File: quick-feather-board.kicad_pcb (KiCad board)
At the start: 4 copper layers, 58.4 x 22.9 mm, 100 parts, among them IC1 EOS-S3-QFN, J1 61300211121, J2 1x12_pinhead, J3 1x16_pinhead, J4 S2B-PH-SM4-TB_LF__SN_, J5 0473460001, J6 FTSH-105-01-L-DV-K, J7 61300211121, J8 2x8_pinhead, M1 mounting_pad, M2 mounting_pad, M3 mounting_pad, M4 mounting_pad, Q1 NX3008CBKV, Q2 2N7002PV, Q3 2N7002PV, Q4 DMG1012T-7, U1 TPS62821DLCR, U2 MCP73831T-2ACI_OT, U3 GD25Q16CWIGR, U4 DPS310, U5 MC3635, X1 ECS-_327-12_5-34B-TR

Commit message: Added board pins description and drawings
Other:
- board text added: "GND HEADER_TX HEADER_RX SPI_MST_MISO SPI_MST_MOSI SPI_MST_CLK S3IO_2 S3IO_13 S3IO_25 S3IO_27 ADC1 n.c. GND n.c. 3V3 SYS_RST"
- board text added: "IO_27 IO_32 IO_33 IO_20 IO_19 IO_17 IO_16 IO_43 IO_3 IO_0 IO_1"
- board text added: "IO_28 IO_23 IO_31 IO_12 IO_5 IO_7 IO_10"
- board text added: "IO_29 IO_24 IO_11 IO_4 IO_8 IO_40"
- board text added: "IO_44 IO_45 IO_36 IO_38 IO_34 IO_2 IO_13 IO_25 IO_27"
- board text added: "PDM_CKO I2S_DOUT S3IO_11 S3IO_4 USR_BUTTON S3IO_8 S3IO_40 GND"
- board text added: "PDM_DATA I2S_WCLK I2S_CLK S3IO_12 S3IO_5 S3IO_7 S3IO_10 3V3"
- board text added: "R IO_22 B IO_18 G IO_21"
- board text added: "VBAT SPI_MST_CS2 S3IO_32_I2C1 S3IO_33_I2C1 SPI_SLV_CSn SPI_SLV_MOSI SPI_SLV_MISO SPI_SLV_CLK HEADER_P6 IMU_INT I2C_SCL I2C_SDA"
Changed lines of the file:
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@@
-(kicad_pcb (version 20171130) (host pcbnew 5.1.4+dfsg1-1~bpo10+1)
+(kicad_pcb (version 20171130) (host pcbnew 5.1.5-52549c5~84~ubuntu18.04.1)
   (general
     (thickness 1.6)
-    (drawings 95)
+    (drawings 104)
     (tracks 1939)
     (zones 0)
@@
   (layers
     (0 Top signal)
-    (1 In1.Cu signal)
-    (2 In2.Cu mixed)
+    (1 In1.Cu signal hide)
+    (2 In2.Cu mixed hide)
     (31 Bottom signal)
     (32 B.Adhes user hide)
@@
     (40 Dwgs.User user hide)
     (41 Cmts.User user hide)
-    (42 Eco1.User user hide)
-    (43 Eco2.User user hide)
+    (42 Eco1.User user)
+    (43 Eco2.User user)
     (44 Edge.Cuts user)
     (45 Margin user hide)
@@
     (visible_elements FFF9FF1F)
     (pcbplotparams
-      (layerselection 0x011fc_ffffffff)
+      (layerselection 0x01d80_7ffffff8)
       (usegerberextensions false)
       (usegerberattributes false)
       (usegerberadvancedattributes false)
       (creategerberjobfile false)
-      (excludeedgelayer true)
+      (excludeedgelayer false)
       (linewidth 0.100000)
       (plotframeref false)
@@
       (psnegative false)
       (psa4output false)
-      (plotreference true)
-      (plotvalue true)
+      (plotreference false)
+      (plotvalue false)
       (plotinvisibletext false)
       (padsonsilk false)
       (subtractmaskfromsilk false)
-      (outputformat 1)
+      (outputformat 4)
       (mirror false)
       (drillshape 0)
@@
     )
   )
+  (gr_text "R IO_22\nB IO_18\nG IO_21" (at 126.8803 89.5517) (layer Eco2.User)
+    (effects (font (size 1.5 1.5) (thickness 0.3)) (justify left))
+  )
+  (gr_text "IO_28\nIO_23\nIO_31\nIO_12\nIO_5\nIO_7\nIO_10\n" (at 182.4603 102.4417) (layer Eco2.User)
+    (effects (font (size 1.5 1.5) (thickness 0.3)) (justify left))
+  )
+  (gr_text "IO_29\nIO_24\nIO_11\nIO_4\n\nIO_8\nIO_40\n\n\n" (at 194.9903 104.9817) (layer Eco2.User)
+    (effects (font (size 1.5 1.5) (thickness 0.3)) (justify left))
+  )
+  (gr_text "PDM_CKO\nI2S_DOUT\nS3IO_11\nS3IO_4\nUSR_BUTTON\nS3IO_8\nS3IO_40\nGND\n\n" (at 194.9803 104.9617) (layer Eco1.User)
+    (effects (font (size 1.5 1.5) (thickness 0.3)) (justify left))
+  )
+  (gr_text "PDM_DATA\nI2S_WCLK\nI2S_CLK\nS3IO_12\nS3IO_5\nS3IO_7\nS3IO_10\n3V3\n\n\n" (at 182.4703 106.2717) (layer Eco1.User)
+    (effects (font (size 1.5 1.5) (thickness 0.3)) (justify left))
+  )
+  (gr_text "GND\nHEADER_TX\nHEADER_RX\nSPI_MST_MISO\nSPI_MST_MOSI\nSPI_MST_CLK\nS3IO_2\nS3IO_13\nS3IO_25\nS3IO_27\nADC1\nn.c.\nGND\nn.c.\n3V3\nSYS_RST" (at 148.3903 116.8917 270) (layer Eco1.User)
+    (effects (font (size 1.5 1.5) (thickness 0.3)) (justify left))
+  )
+  (gr_text "IO_44\nIO_45\nIO_36\nIO_38\nIO_34\nIO_2\nIO_13\nIO_25\nIO_27\n" (at 154.7403 116.8917 270) (layer Eco2.User)
+    (effects (font (size 1.5 1.5) (thickness 0.3)) (justify left))
+  )
+  (gr_text "IO_27\nIO_32\nIO_33\nIO_20\nIO_19\nIO_17\nIO_16\nIO_43\nIO_3\nIO_0\nIO_1" (at 154.9003 93.1917 90) (layer Eco2.User)
+    (effects (font (size 1.5 1.5) (thickness 0.3)) (justify left))
+  )
+  (gr_text "VBAT\nSPI_MST_CS2\nS3IO_32_I2C1\nS3IO_33_I2C1\nSPI_SLV_CSn\nSPI_SLV_MOSI\nSPI_SLV_MISO\nSPI_SLV_CLK\nHEADER_P6\nIMU_INT\nI2C_SCL\nI2C_SDA" (at 153.6103 93.1917 90) (layer Eco1.User)
+    (effects (font (size 1.5 1.5) (thickness 0.3)) (justify left))
+  )
   (gr_text Prototype (at 164.311 111.443) (layer B.SilkS)

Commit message: Corrected IO_27 to IO_30
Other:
- board text added: "GND HEADER_TX HEADER_RX SPI_MST_MISO SPI_MST_MOSI SPI_MST_CLK S3IO_2 S3IO_13 S3IO_25 S3IO_30 ADC1 n.c. GND n.c. 3V3 SYS_RST"
- board text added: "IO_44 IO_45 IO_36 IO_38 IO_34 IO_2 IO_13 IO_25 IO_30"
- board text removed: "GND HEADER_TX HEADER_RX SPI_MST_MISO SPI_MST_MOSI SPI_MST_CLK S3IO_2 S3IO_13 S3IO_25 S3IO_27 ADC1 n.c. GND n.c. 3V3 SYS_RST"
- board text removed: "IO_44 IO_45 IO_36 IO_38 IO_34 IO_2 IO_13 IO_25 IO_27"
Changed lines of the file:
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@@
     (effects (font (size 1.5 1.5) (thickness 0.3)) (justify left))
   )
-  (gr_text "GND\nHEADER_TX\nHEADER_RX\nSPI_MST_MISO\nSPI_MST_MOSI\nSPI_MST_CLK\nS3IO_2\nS3IO_13\nS3IO_25\nS3IO_27\nADC1\nn.c.\nGND\nn.c.\n3V3\nSYS_RST" (at 148.3903 116.8917 270) (layer Eco1.User)
+  (gr_text "GND\nHEADER_TX\nHEADER_RX\nSPI_MST_MISO\nSPI_MST_MOSI\nSPI_MST_CLK\nS3IO_2\nS3IO_13\nS3IO_25\nS3IO_30\nADC1\nn.c.\nGND\nn.c.\n3V3\nSYS_RST" (at 148.3903 116.8917 270) (layer Eco1.User)
     (effects (font (size 1.5 1.5) (thickness 0.3)) (justify left))
   )
-  (gr_text "IO_44\nIO_45\nIO_36\nIO_38\nIO_34\nIO_2\nIO_13\nIO_25\nIO_27\n" (at 154.7403 116.8917 270) (layer Eco2.User)
+  (gr_text "IO_44\nIO_45\nIO_36\nIO_38\nIO_34\nIO_2\nIO_13\nIO_25\nIO_30\n" (at 154.7403 116.8917 270) (layer Eco2.User)
     (effects (font (size 1.5 1.5) (thickness 0.3)) (justify left))
   )

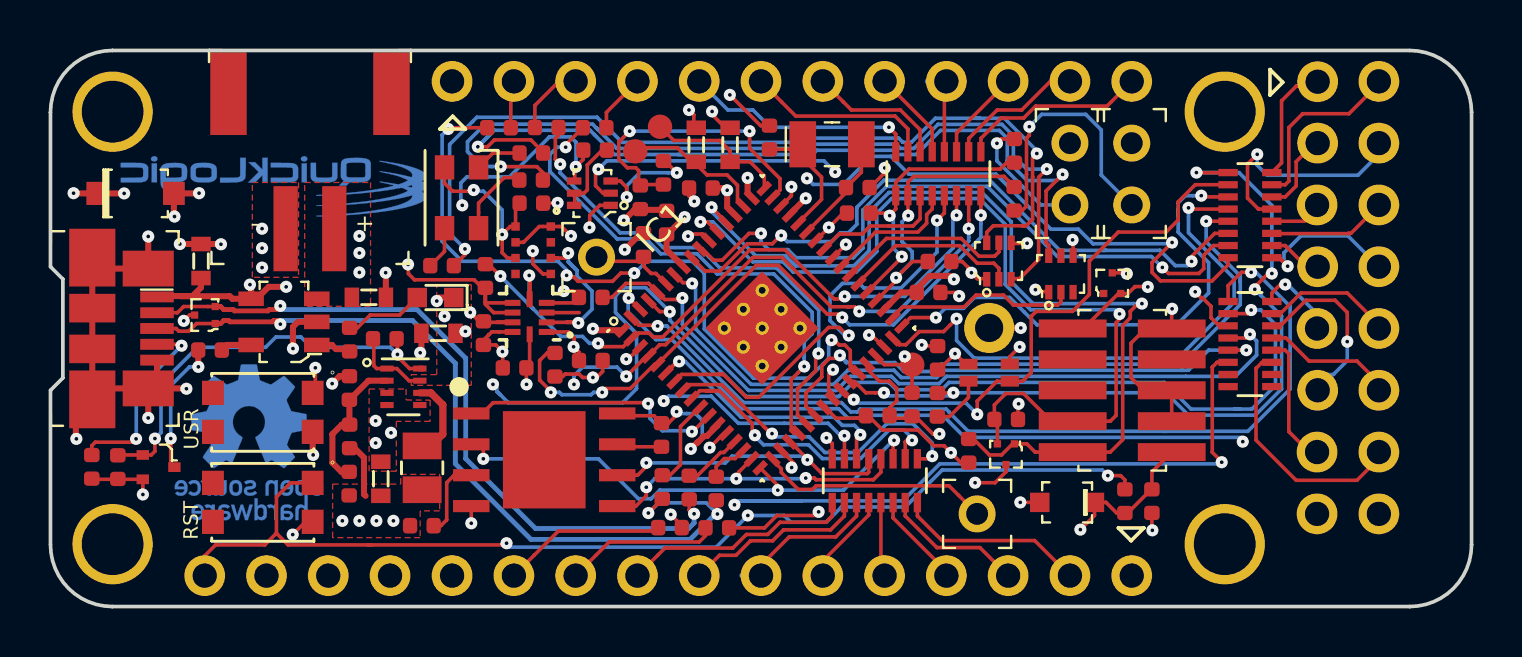
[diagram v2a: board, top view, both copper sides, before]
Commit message: Added plots for fabrication layers
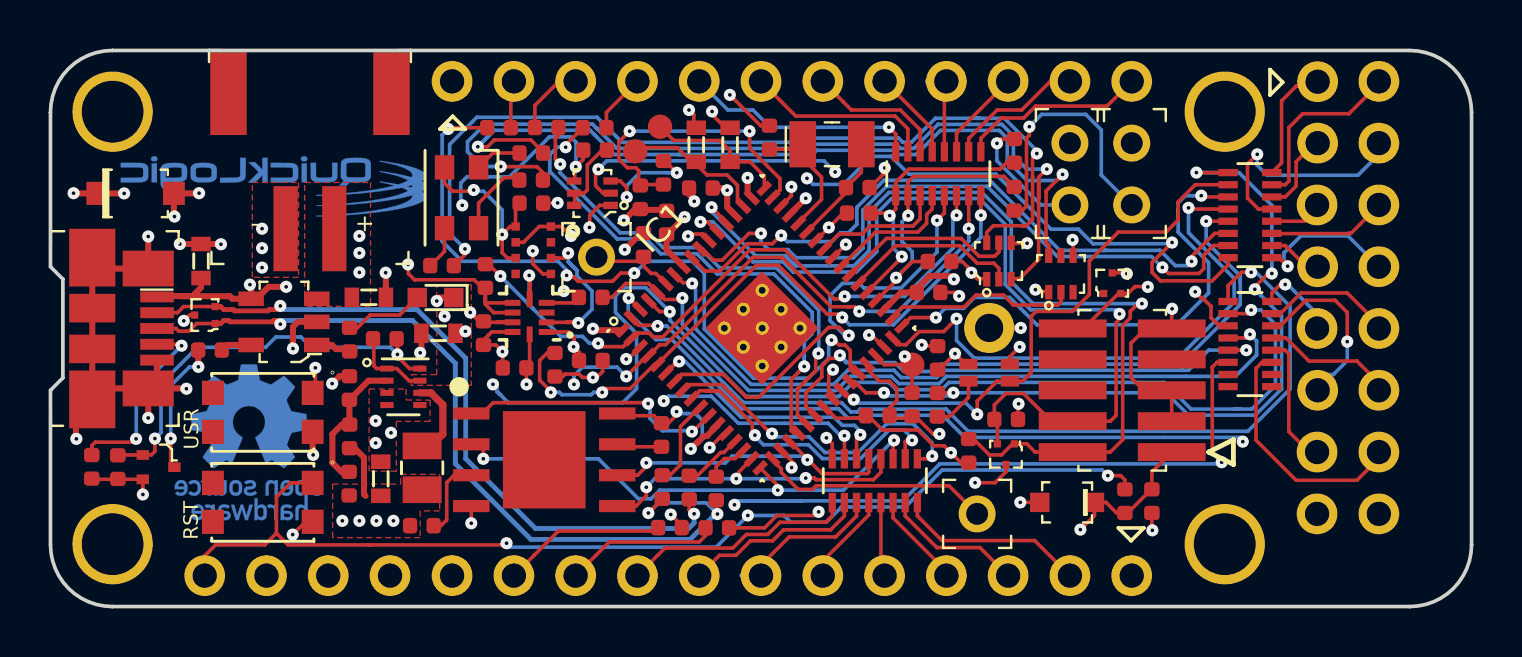
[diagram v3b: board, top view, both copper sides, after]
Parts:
- moved U4 2.33 mm to (142.9, 101.8)
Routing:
- net Net-(U5-Pad3): track 1.34 -> 0.00 mm

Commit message: Added description for PCB finish
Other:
- board text added: "2"
- board text added: "3"
- board text added: "4"
- board text added: "5"
- board text added: "6"
- board text added: "7"
- board text added: "8"
- board text added: "9"
- board text added: "Prepreg"
- board text added: "Recommended PCB finish: Gold plating (ENIG, selective) Solder mask: matt black Silkscreen: white"
- board text added: "The design does not include high speed signalling. No impedance control is required. Suggested prepreg material is ISOLA PR2116"
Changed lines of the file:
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@@
   (general
     (thickness 1.6)
-    (drawings 104)
+    (drawings 108)
     (tracks 1938)
     (zones 0)
@@
     (38 B.Mask user hide)
     (39 F.Mask user hide)
-    (40 Dwgs.User user hide)
+    (40 Dwgs.User user)
     (41 Cmts.User user hide)
     (42 Eco1.User user hide)
@@
       (drillshape 0)
       (scaleselection 1)
-      (outputdirectory "pcb"))
+      (outputdirectory "doc"))
   )
   (net 0 "")
@@
     )
   )
+  (gr_text Prepreg (at 209.601 111.243) (layer Dwgs.User)
+    (effects (font (size 1 1) (thickness 0.15)))
+  )
+  (gr_text Prepreg (at 209.601 103.333) (layer Dwgs.User)
+    (effects (font (size 1 1) (thickness 0.15)))
+  )
+  (gr_text "The design does not include high speed signalling.\nNo impedance control is required.\nSuggested prepreg material is ISOLA PR2116\n" (at 185.6603 126.3217) (layer Dwgs.User)
+    (effects (font (size 0.7 0.7) (thickness 0.1)) (justify left))
+  )
+  (gr_text "Recommended PCB finish:\nGold plating (ENIG, selective)\nSolder mask: matt black\nSilkscreen: white" (at 185.4803 121.2717) (layer Dwgs.User)
+    (effects (font (size 1 1) (thickness 0.15)) (justify left))
+  )
   (gr_text "R IO_22\nB IO_18\nG IO_21" (at 126.8803 89.5517) (layer Eco2.User)
     (effects (font (size 1.5 1.5) (thickness 0.3)) (justify left))
@@
     (effects (font (size 1 1) (thickness 0.15)))
   )
-  (gr_text 1 (at 189.701 115.213) (layer Dwgs.User)
+  (gr_text 9 (at 189.701 115.213) (layer Dwgs.User)
     (effects (font (size 1 1) (thickness 0.15)))
   )
-  (gr_text 1 (at 189.701 113.213) (layer Dwgs.User)
+  (gr_text 8 (at 189.701 113.213) (layer Dwgs.User)
     (effects (font (size 1 1) (thickness 0.15)))
   )
-  (gr_text 1 (at 189.701 111.213) (layer Dwgs.User)
+  (gr_text 7 (at 189.701 111.213) (layer Dwgs.User)
     (effects (font (size 1 1) (thickness 0.15)))
   )
-  (gr_text 1 (at 189.701 109.213) (layer Dwgs.User)
+  (gr_text 6 (at 189.701 109.213) (layer Dwgs.User)
     (effects (font (size 1 1) (thickness 0.15)))
   )
-  (gr_text 1 (at 189.701 107.213) (layer Dwgs.User)
+  (gr_text 5 (at 189.701 107.213) (layer Dwgs.User)
     (effects (font (size 1 1) (thickness 0.15)))
   )
-  (gr_text 1 (at 189.701 105.213) (layer Dwgs.User)
+  (gr_text 4 (at 189.701 105.213) (layer Dwgs.User)
     (effects (font (size 1 1) (thickness 0.15)))
   )
-  (gr_text 1 (at 189.701 103.213) (layer Dwgs.User)
+  (gr_text 3 (at 189.701 103.213) (layer Dwgs.User)
     (effects (font (size 1 1) (thickness 0.15)))
   )
-  (gr_text 1 (at 189.701 101.213) (layer Dwgs.User)
+  (gr_text 2 (at 189.701 101.213) (layer Dwgs.User)
     (effects (font (size 1 1) (thickness 0.15)))
   )
